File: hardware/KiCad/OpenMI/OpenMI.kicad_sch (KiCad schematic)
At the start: 0 parts

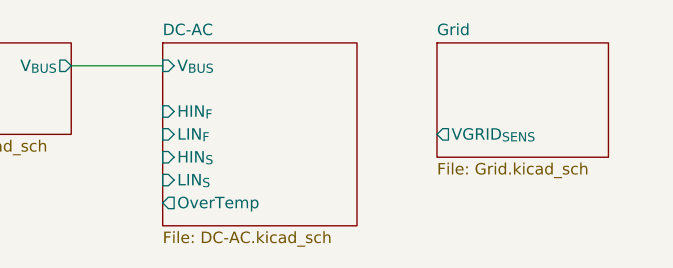
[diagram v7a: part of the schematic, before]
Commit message: fix(hw): Fix hierarchical label direction
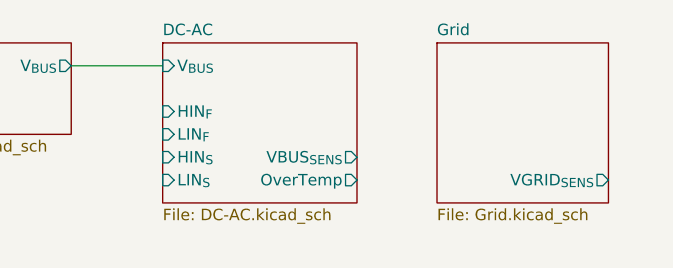
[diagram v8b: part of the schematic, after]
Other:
- sheet DC-AC ports: added VBUS_{SENS}; removed none
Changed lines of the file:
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@@
     (stroke (width 0) (type default))
   )
-  (sheet (at 154.94 83.82) (size 21.59 20.32) (fields_autoplaced)
+  (sheet (at 154.94 83.82) (size 21.59 17.78) (fields_autoplaced)
     (stroke (width 0.1524) (type solid))
     (fill (color 0 0 0 0.0000))
@@
       (effects (font (size 1.27 1.27)) (justify left bottom))
     )
-    (property "Sheetfile" "DC-AC.kicad_sch" (at 154.94 104.7246 0)
+    (property "Sheetfile" "DC-AC.kicad_sch" (at 154.94 102.1846 0)
       (effects (font (size 1.27 1.27)) (justify left top))
     )
@@
       (effects (font (size 1.27 1.27)) (justify left))
     )
-    (pin "OverTemp" output (at 154.94 101.6 180)
-      (effects (font (size 1.27 1.27)) (justify left))
+    (pin "OverTemp" output (at 176.53 99.06 0)
+      (effects (font (size 1.27 1.27)) (justify right))
     )
     (pin "V_{BUS}" input (at 154.94 86.36 180)
       (effects (font (size 1.27 1.27)) (justify left))
+    )
+    (pin "VBUS_{SENS}" output (at 176.53 96.52 0)
+      (effects (font (size 1.27 1.27)) (justify right))
     )
     (instances
@@
     )
   )
-  (sheet (at 185.42 83.82) (size 19.05 12.7) (fields_autoplaced)
+  (sheet (at 185.42 83.82) (size 19.05 17.78) (fields_autoplaced)
     (stroke (width 0.1524) (type solid))
     (fill (color 0 0 0 0.0000))
@@
       (effects (font (size 1.27 1.27)) (justify left bottom))
     )
-    (property "Sheetfile" "Grid.kicad_sch" (at 185.42 97.1046 0)
+    (property "Sheetfile" "Grid.kicad_sch" (at 185.42 102.1846 0)
       (effects (font (size 1.27 1.27)) (justify left top))
     )
@@
       (effects (font (size 1.27 1.27)) hide)
     )
-    (pin "VGRID_{SENS}" output (at 185.42 93.98 180)
-      (effects (font (size 1.27 1.27)) (justify left))
+    (pin "VGRID_{SENS}" output (at 204.47 99.06 0)
+      (effects (font (size 1.27 1.27)) (justify right))
     )
     (instances
